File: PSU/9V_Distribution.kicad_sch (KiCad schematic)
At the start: 20 parts, among them J1 Screw_Terminal_2_P5.00mm, J2 Screw_Terminal_2_P5.00mm, J3 Screw_Terminal_2_P5.00mm, J4 Screw_Terminal_2_P5.00mm, U4 LM2596S-5

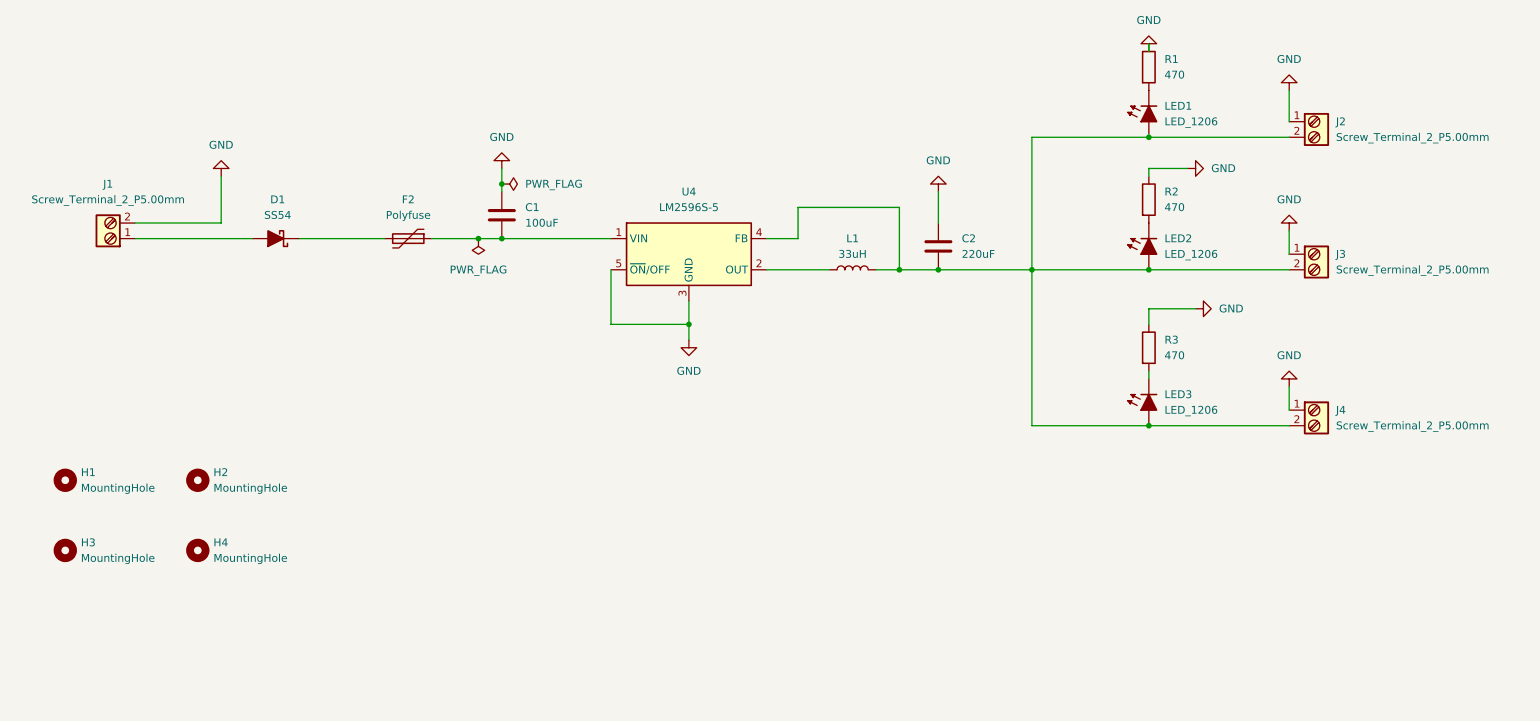
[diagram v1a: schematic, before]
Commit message: Give the PSU buck the catch diode it never had
The LM2596 on the 9V distribution board has been running without a
freewheel diode. Net-(U4-OUT) held exactly two nodes, U4.2 and L1.1: the
only Schottky on the board is D1, in series at the input as reverse
protection. With nowhere else to go, the inductor current has been
freewheeling through the regulator's own substrate diode, adding roughly
0.4 W inside the package on top of its own 0.7 W. That is why the board
works, and why it wears out.

  D2  SS54 Schottky, cathode on the switch node, anode to ground.
  C4  220uF electrolytic beside C2, to give the control loop the ESR a
      ceramic output capacitor does not provide.
  F2  MF-RHT100 -> MF-RHT200. The input draws ~0.75 A and a 1 A polyfuse
      derates below 0.8 A in a warm printed case. Identical pads.

The power section is re-laid out around this. U4 pin 2, D2's cathode and
L1 pin 1 now sit on one straight line at y=64.95, and C1 moved under the
VIN pin, flipped so its ground terminal faces D2's anode. Every track is
on the front, so the bottom stays an uninterrupted ground plane and each
loop's return runs directly beneath its outward track. Stitching vias at
the ground terminals connect to their pads by track, not through thermal
spokes.

Outline, mounting holes and J1-J4 are untouched: same case, same wiring.

0 unconnected items, 0 schematic parity issues. DRC still reports the
stale ground pour until the zone is refilled in Pcbnew; with the fill
polygons stripped, clearance, hole and solder-mask checks are all clean
and only the pre-existing missing-library warnings remain.

The board in service is still the old one. The Readme says what to bodge
onto it in the meantime.

Co-Authored-By: Claude Opus 5 <noreply@anthropic.com>
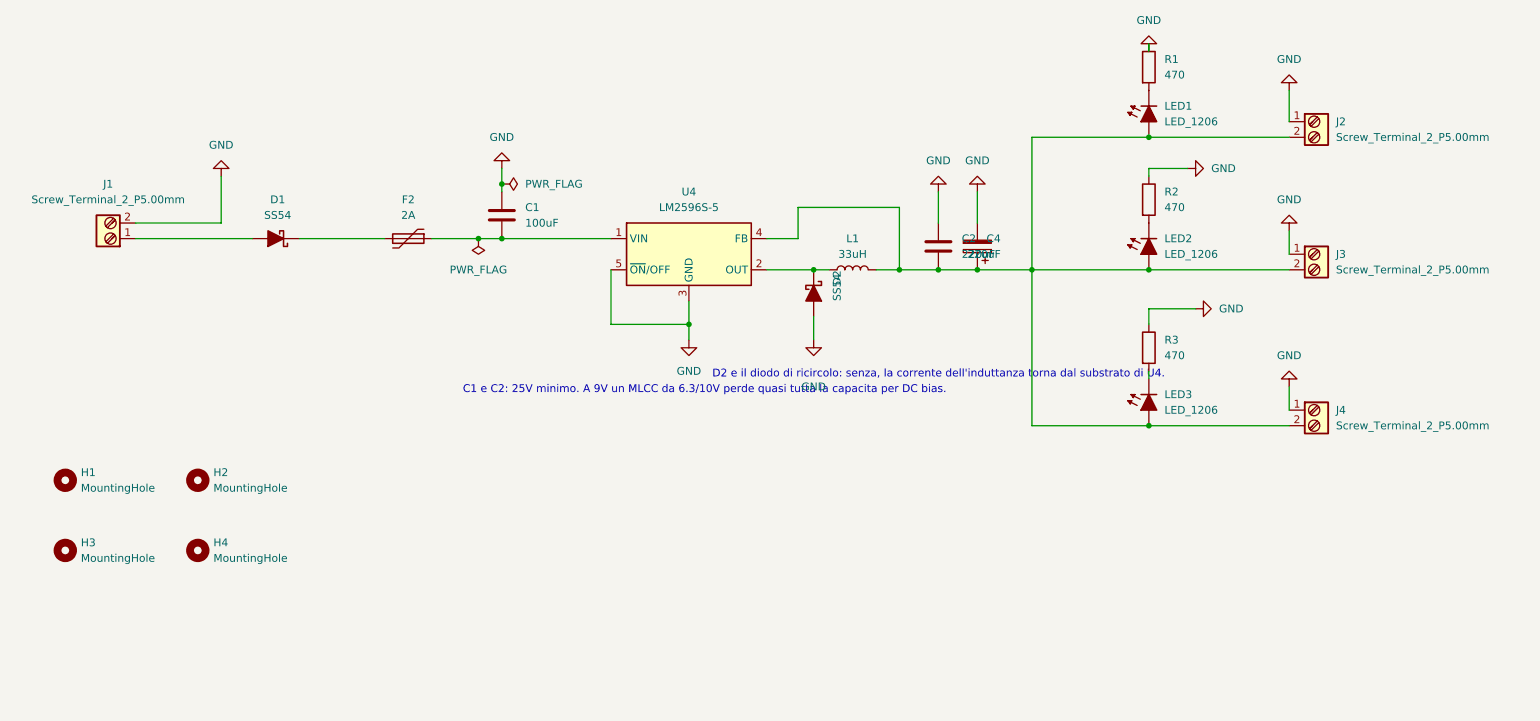
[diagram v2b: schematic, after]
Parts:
- added C4: 220uF, Capacitor_THT:CP_Radial_D6.3mm_P2.50mm, symbol Device:C_Polarized
- added D2: SS54, PCM_Diode_SMD_AKL:D_SMC, symbol PCM_Diode_Schottky_AKL:SS54
- F2: value Polyfuse -> 2A; footprint Fuse:Fuse_Bourns_MF-RHT100 -> Fuse:Fuse_Bourns_MF-RHT200
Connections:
- net GND: now also C4.2, D2.2 (A)
- net at L1.1, U4.2 (OUT): now also D2.1 (K)
- net at C2.2, J2.2, J3.2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: now also C4.1
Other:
- note added: "C1 e C2: 25V minimo. A 9V un MLCC da 6.3/10V perde quasi tutta la capacita per DC bias."
- note added: "D2 e il diodo di ricircolo: senza, la corrente dell'induttanza torna dal substrato di U4."

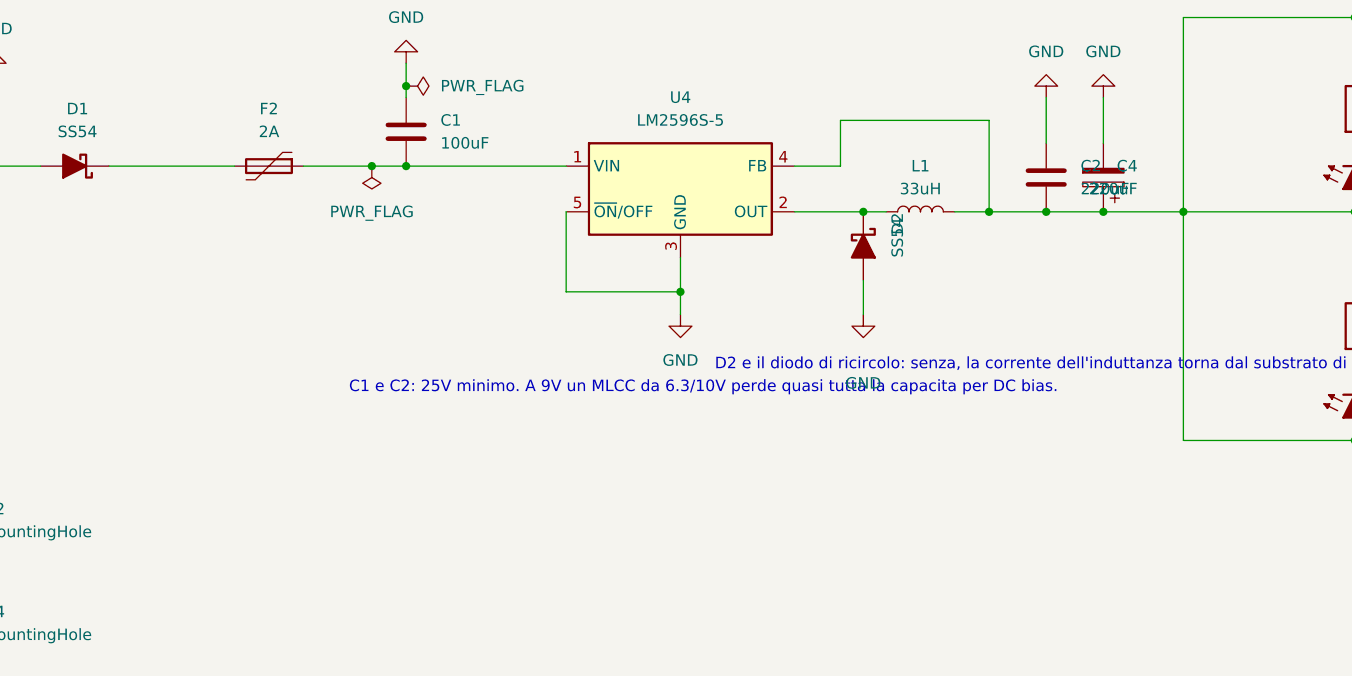
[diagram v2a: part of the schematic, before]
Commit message: Add the mainboard 9V branch to the PSU
Second, independent regulator on the PSU so the mainboard does not share a
rail with the PWM-switched backlighting. Tapped from D1's cathode: the
reverse protection is shared, the fuse is not, so a fault on one branch
does not take down the other.

  F3  0.5A polyfuse, mainboard branch only
  U1  P78A05-1000, the same module already used on RMP V5
  C5/C6, C7/C8  100nF + 100uF each side, mirroring RMP V5
  J5  screw terminal, beside J1, so both cables leave the same edge

Nets are labelled VIN_MB and +5V_MB rather than left as Net-(U1-+VOUT).

Layout: the whole chain sits in the y 44..56 band, which was empty. That
band was empty of footprints but not of copper -- the buck's output
distribution ran through it to reach J2/J3/J4. That distribution now runs
on a spine above the band at y 44.8 and crosses to the bottom half through
a single 13mm bottom-layer link at x 144.5, well away from the switching
loop. Everything else stays on the front, so the ground plane keeps one
narrow slot and nothing more.

The 9V climbs the left edge in the 2mm corridor between the board edge and
U4's tab; the 5V descends the right edge to J5. C4 moved 1.5mm to clear
the terminal.

0 unconnected items, 0 schematic parity issues, no silkscreen violations.
DRC reports the stale ground pour until the zone is refilled in Pcbnew:
79 of the 95 violations name it, the other 16 are the pre-existing library
links.

Co-Authored-By: Claude Opus 5 <noreply@anthropic.com>
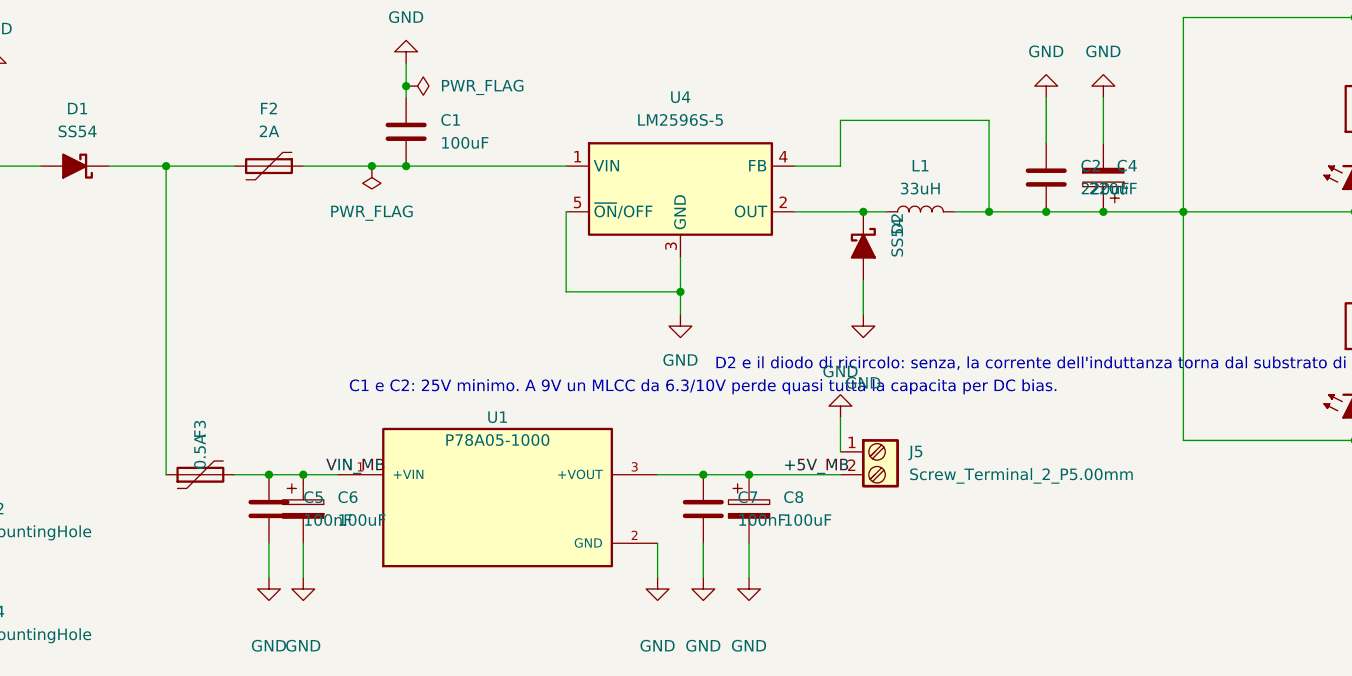
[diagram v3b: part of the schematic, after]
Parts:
- added C5, C7: 100nF, Capacitor_SMD:C_1206_3216Metric_Pad1.33x1.80mm_HandSolder, symbol Device:C
- added C6, C8: 100uF, Capacitor_THT:CP_Radial_D6.3mm_P2.50mm, symbol Device:C_Polarized
- added F3: 0.5A, Fuse:Fuse_Bourns_MF-RHT050, symbol Device:Polyfuse
- added J5: Screw_Terminal_2_P5.00mm, TerminalBlock_Phoenix:TerminalBlock_Phoenix_PT-1,5-2-5.0-H_1x02_P5.00mm_Horizontal, symbol PCM_SL_Screw_Terminal:Screw_Terminal_2_P5.00mm
- added U1: P78A05-1000, Custom_Footprints:CONV_P78A05-1000, symbol P78A05-1000:P78A05-1000
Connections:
- net GND: now also C5.2, C6.2, C7.2, C8.2, J5.1, U1.2 (GND)
- net at D1.1 (K), F2.2: now also F3.1
- new net +5V_MB: C7.1, C8.1, J5.2, U1.3 (+VOUT)
- new net VIN_MB: C5.1, C6.1, F3.2, U1.1 (+VIN)

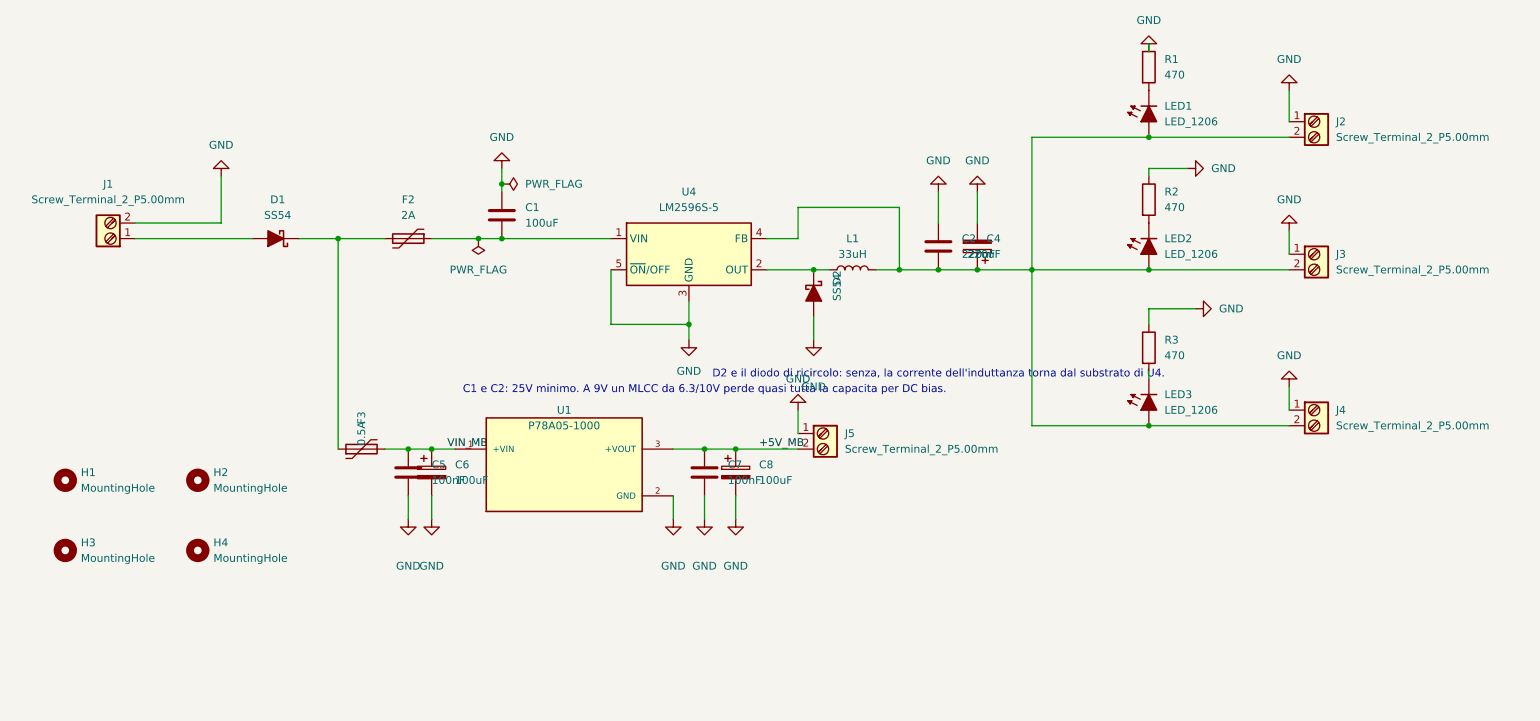
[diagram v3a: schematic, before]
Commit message: Turn J5 round and move the PSU notes clear of the drawing
J5 was placed with its wire entry facing C8, leaving no room for the
cables. Rotated 180 and moved to (160, 33) so the cables leave over the
top edge, the same way J2-J4 do. The output track follows pad 2 to its new
position.

The two schematic notes sat on top of each other and over U1's fields.
They move below the drawing, which ends at y 127, and become four:
the two supply branches, the shared reverse protection with separate
fuses, what D2 is for, and C1's voltage rating. The old note claimed C2
needed 25 V as well; it does not, it sits on the 5 V output.

Includes the zone refill done in Pcbnew, which brought the board to 16
violations, all library links, with 0 unconnected and 0 parity issues.
Moving J5 makes the pour stale again for 8 of them, so it needs one more
refill.

Co-Authored-By: Claude Opus 5 <noreply@anthropic.com>
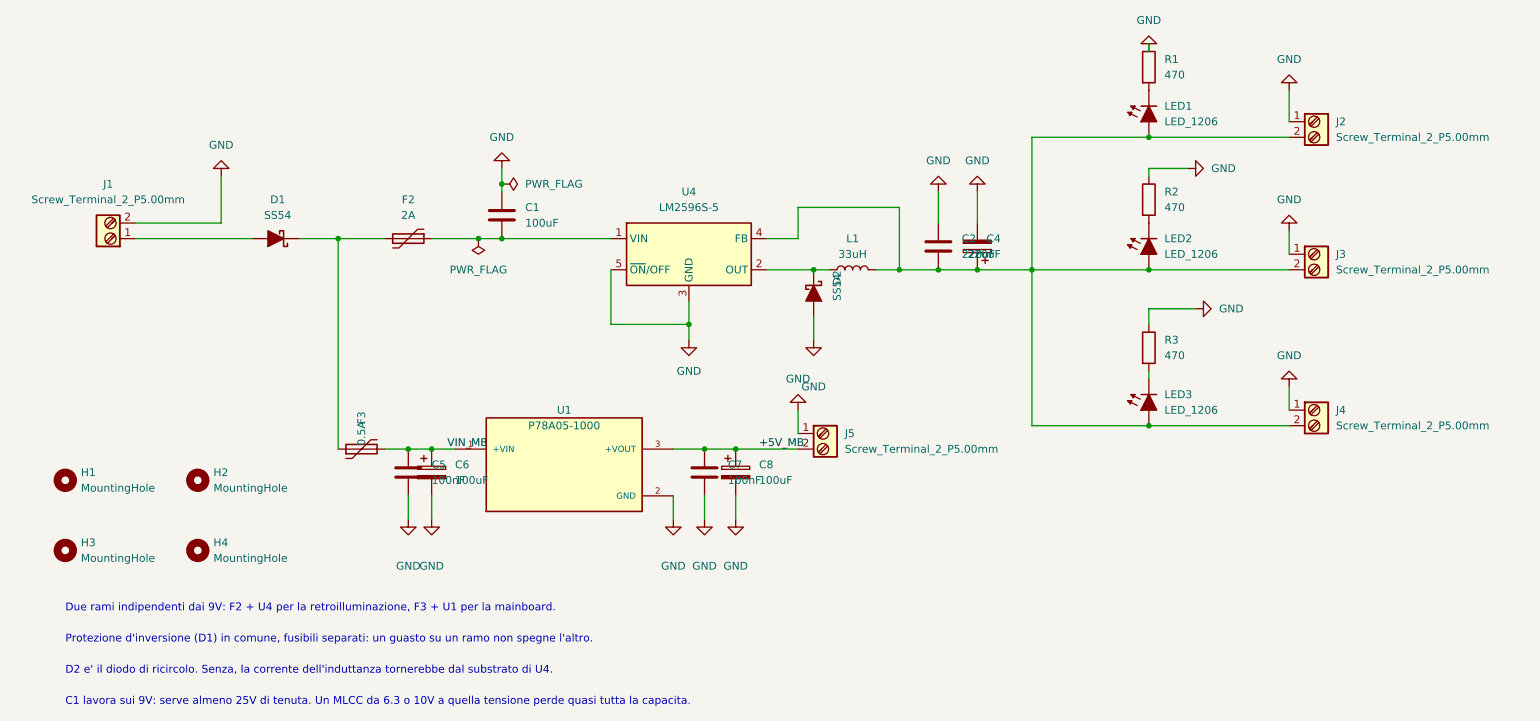
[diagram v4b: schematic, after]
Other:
- note added: "C1 lavora sui 9V: serve almeno 25V di tenuta. Un MLCC da 6.3 o 10V a quella tensione perde quasi tutta la capacita."
- note added: "D2 e' il diodo di ricircolo. Senza, la corrente dell'induttanza tornerebbe dal substrato di U4."
- note added: "Due rami indipendenti dai 9V: F2 + U4 per la retroilluminazione, F3 + U1 per la mainboard."
- note added: "Protezione d'inversione (D1) in comune, fusibili separati: un guasto su un ramo non spegne l'altro."
- note removed: "C1 e C2: 25V minimo. A 9V un MLCC da 6.3/10V perde quasi tutta la capacita per DC bias."
- note removed: "D2 e il diodo di ricircolo: senza, la corrente dell'induttanza torna dal substrato di U4."
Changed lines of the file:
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@@
 		(color 0 0 0 0)
-	)
-	(text "C1 e C2: 25V minimo. A 9V un MLCC da 6.3/10V perde quasi tutta la capacita per DC bias."
-		(exclude_from_sim no)
-		(at 96.52 101.6 0)
-		(effects
-			(font
-				(size 1.27 1.27)
-			)
-			(justify left bottom)
-		)
-	)
-	(text "D2 e il diodo di ricircolo: senza, la corrente dell'induttanza torna dal substrato di U4."
-		(exclude_from_sim no)
-		(at 137.16 99.06 0)
-		(effects
-			(font
-				(size 1.27 1.27)
-			)
-			(justify left bottom)
-		)
 	)
 	(symbol
@@
 		(effects
 			(font
+				(size 1.27 1.27)
+			)
+			(justify left bottom)
+		)
+	)
+	(text "Due rami indipendenti dai 9V: F2 + U4 per la retroilluminazione, F3 + U1 per la mainboard."
+		(exclude_from_sim no)
+		(at 31.75 137.16 0)
+		(effects
+			(font
+				(size 1.27 1.27)
+			)
+			(justify left bottom)
+		)
+	)
+	(text "Protezione d'inversione (D1) in comune, fusibili separati: un guasto su un ramo non spegne l'altro."
+		(exclude_from_sim no)
+		(at 31.75 142.24 0)
+		(effects
+			(font
+				(size 1.27 1.27)
+			)
+			(justify left bottom)
+		)
+	)
+	(text "D2 e' il diodo di ricircolo. Senza, la corrente dell'induttanza tornerebbe dal substrato di U4."
+		(exclude_from_sim no)
+		(at 31.75 147.32 0)
+		(effects
+			(font
+				(size 1.27 1.27)
+			)
+			(justify left bottom)
+		)
+	)
+	(text "C1 lavora sui 9V: serve almeno 25V di tenuta. Un MLCC da 6.3 o 10V a quella tensione perde quasi tutta la capacita."
+		(exclude_from_sim no)
+		(at 31.75 152.4 0)
+		(effects
+			(font
